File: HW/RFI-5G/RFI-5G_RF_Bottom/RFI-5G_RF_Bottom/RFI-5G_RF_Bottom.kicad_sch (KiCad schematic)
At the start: 20 parts, among them J1 Conn_01x10, J2 Conn_01x10, J3 Conn_01x10, J4 Conn_01x10, J5 SMP, J6 Conn_01x04_Female

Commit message: RF top and Bottom boards
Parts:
- removed J1, J2, J3: Conn_01x10, symbol Connector_Generic:Conn_01x10
- removed J6: Conn_01x04_Female, Connector_PinHeader_2.54mm:PinHeader_1x04_P2.54mm_Vertical, symbol Connector:Conn_01x04_Female
- removed U?: LEE2-6+, Package_SON:WSON-6-1EP_2x2mm_P0.65mm_EP1x1.6mm, symbol GGS_RF:LEE2-6+
- added C1, C5: 100nF, Capacitor_SMD:C_0402_1005Metric, symbol Device:C
- added C10, C6: 1uF, Capacitor_SMD:C_0402_1005Metric, symbol Device:C
- added C11, C12, C2, C4, C7: 10nF, Capacitor_SMD:C_0402_1005Metric, symbol Device:C
- added C18: 10uF, Capacitor_SMD:C_0402_1005Metric, symbol Device:C
- added FL1: LFCW-8400+, GGS_RF:JC0603C-1, symbol GGS_RF:LFCW-8000+
- added FL2: HFCN-5500+, GGS_RF:JC0603C, symbol GGS_RF:HFCN-5500+
- added FL3: SAW_869, GGS_RF:QCS5P, symbol GGS_RF:SAW_869
- added J1, J3: Conn_01x03, Connector_PinHeader_2.54mm:PinHeader_1x03_P2.54mm_Vertical, symbol Connector_Generic:Conn_01x03
- added J2: Conn_01x02, Connector_PinHeader_2.54mm:PinHeader_1x02_P2.54mm_Vertical, symbol Connector_Generic:Conn_01x02
- added J6: Conn_01x06_Female, Connector_PinHeader_1.00mm:PinHeader_1x06_P1.00mm_Vertical, symbol Connector:Conn_01x06_Female
- added L1: 0.9uH, Inductor_SMD:L_0603_1608Metric, symbol Device:L
- added L2: 590nH, Inductor_SMD:L_0603_1608Metric, symbol Device:L
- added L3: 120nH, Inductor_SMD:L_0603_1608Metric, symbol Device:L
- added R1: 3k, Resistor_SMD:R_0603_1608Metric, symbol Device:R
- added R2: 43R, Resistor_SMD:R_0603_1608Metric, symbol Device:R
- added R3: 88R7, Resistor_SMD:R_0603_1608Metric, symbol Device:R
- added U1: HMC8411, GGS_RF:6-LFCSP, symbol GGS_RF:HMC8411
- added U2: SIM-14+, GGS_RF:HV1195, symbol GGS_RF:SIM-14+
- added U4: LEE2-6+, Package_SON:WSON-6-1EP_2x2mm_P0.65mm_EP1x1.6mm, symbol GGS_RF:LEE2-6+
- added U7: HMC358, Package_SO:MSOP-8-1EP_3x3mm_P0.65mm_EP2.5x3mm_Mask1.73x2.36mm, symbol GGS_RF:HMC358
- C8: renamed from C?; value C -> 1uF
- C9: renamed from C?; value C -> 10nF
- J4: footprint (none) -> Connector_PinHeader_2.54mm:PinHeader_1x10_P2.54mm_Vertical
- J5: footprint easyeda:CES-110-XX-Y-S -> GGS_Connectors:SMP_StraightPlugPCB
- L4: renamed from L?; value L -> 120nH; footprint (none) -> Inductor_SMD:L_0603_1608Metric
- L5: renamed from L?; footprint (none) -> Inductor_SMD:L_0603_1608Metric
- R4: renamed from R?; value R -> 88R7; footprint (none) -> Resistor_SMD:R_0603_1608Metric
- R5: renamed from R?; footprint (none) -> Resistor_SMD:R_0603_1608Metric
- gave numbers to parts that had none: 7
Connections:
- net CHGOFF is gone; now on net Vcc_IF2Amp2: J4.7 (Pin_7)
- net CLPROG is gone; now on net 3V: J4.8 (Pin_8)
- net MPPT_X is gone; now on net RSSI_Out: J4.9 (Pin_9)
- net SOLAR_X is gone; now on net GND: J4.10 (Pin_10)
- net SWCLK is gone; now on net GND: J4.4 (Pin_4)
- net ADC_PL2: now also J3.2 (Pin_2); no longer J4.2 (Pin_2)
- net DAC_PL2: now also J3.3 (Pin_3); no longer J4.3 (Pin_3)
- net GND: now also J4.3 (Pin_3), U5.1 (NC), U5.3 (NC), U5.4 (NC), U5.6 (NC), U5.7 (NC), C1.1, C10.1, C11.1, C18.1, C2.1, C5.1, C6.1, C7.1, FL1.2 (GND), FL1.4 (GND), FL2.2 (GND), FL2.4 (GND), FL2.5 (GND), FL2.6 (GND), FL3.2 (GND), FL3.3 (GND), FL3.5 (GND), J1.3 (Pin_3), J2.1 (Pin_1), J3.1 (Pin_1), U1.3 (NC), U1.4 (NC), U1.6 (GND), U2.1 (GND), U4.1 (NC), U4.3 (NC), U4.4 (NC), U4.6 (NC), U4.7 (NC), U7.2 (NC), U7.4 (GND), U7.5 (GND), U7.6 (NC), U7.7 (NC), U7.9 (GND)
- net SCL: now also J1.2 (Pin_2)
- net SDA: now also J1.1 (Pin_1)
- net VCC: now also J2.2 (Pin_2)
- net LEE_2_Out: now reaches C13.1, L4.2, U5.5 (Out&DCin)
- net Vcc_IF2Amp2: now reaches C8.2, C9.2, R4.1
- net 3V: now reaches U3.1 (ENBL)
- net 3V: now also U3.6 (VCC), C10.2, C11.2
- net RSSI_In+: now reaches C14.2, U3.2 (IN+)
- net RSSI_IN-: now reaches C17.2, U3.3 (IN-)
- net RSSI_Out: now reaches U3.8 (OUT)
- net SAW_Out: now reaches U5.2 (In)
- net SAW_Out: now also FL3.4 (Out)
- net NRST renamed Vcc_IF2Amp1
- net Vcc_IF2Amp1: now also C6.2, C7.2, R3.1
- net PCLK renamed Vcc_VCO
- net Vcc_VCO: now also C18.2, J6.6 (Pin_6), U7.1 (Vcc)
- net RF_Bottom_In renamed IF1_In
- net IF1_In: now also FL2.1 (In)
- net SWIO renamed PoL
- new net: L3.1, R3.2
- new net: L2.2, R2.1
- new net: C5.2, R2.2
- new net: R1.2, U1.1 (RBIAS)
- new net IF1_Amp_Out: C4.1, L1.2, U1.5 (RFOut)
- new net IF1_HPF_Out: FL2.3 (Out), L2.1, U1.2 (RFIn)
- new net IF1_LPF_In: C4.2, FL1.1 (In)
- new net IF1_Out: FL1.3 (Out), U2.4 (RF)
- new net IF2_Amp1_Out: C12.1, L3.2, U4.5 (Out&DCin)
- new net LO2: U2.8 (LO), U7.8 (RFOut)
- new net Mixer_Out: U2.2 (IF), U4.2 (In)
- new net SAW_In: C12.2, FL3.1 (In)
- new net VTune1: J6.1 (Pin_1)
- new net VTune2: J4.2 (Pin_2), U7.3 (VTune)
- new net Vcc_IF1Amp: C1.2, C2.2, J6.3 (Pin_3), L1.1, R1.1
- new net Vcc_LNA1: J6.4 (Pin_4)
- new net Vcc_LNA2: J6.5 (Pin_5)
- new net Vcc_LO1Amp: J6.2 (Pin_2)
- no-connect marks 11 -> 0
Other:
- note added: "IF 1"
- note added: "IF 2"
- note added: "Local Oscillator 2"
- note added: "PoquetQube Connectors"
- note added: "RF Connector"
- note added: "Through-board Pins"
- moved on the sheet: C13, C14, C15, C16, C17, C8, C9, J5, L4, L5, R4, R5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

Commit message: PL boards
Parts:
- removed J6: Conn_01x06_Female, Connector_PinHeader_1.00mm:PinHeader_1x06_P1.00mm_Vertical, symbol Connector:Conn_01x06_Female
- added J6: Conn_01x10_Female, Connector_PinHeader_1.00mm:PinHeader_1x10_P1.00mm_Vertical, symbol Connector:Conn_01x10_Female
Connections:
- net 3V: now also J6.8 (Pin_8)
- net GND: now also J6.7 (Pin_7)
- net SCL: now also J6.10 (Pin_10)
- net SDA: now also J6.9 (Pin_9)
- net VTune1: now also J6.2 (Pin_2)
- net Vcc_IF1Amp: now also J6.1 (Pin_1)
- net Vcc_LNA1: now also J6.6 (Pin_6)
- net Vcc_LNA2: now also J6.5 (Pin_5)
- net Vcc_LO1Amp: now also J6.4 (Pin_4)
- net Vcc_VCO: now also J6.3 (Pin_3)
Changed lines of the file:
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@@
+    (stroke (width 0) (type default) (color 0 0 0 0))
+  )
+  (wire (pts (xy 104.14 148.59) (xy 111.76 148.59))
     (stroke (width 0) (type default) (color 0 0 0 0))
   )
@@
     (effects (font (size 1.27 1.27)) (justify left bottom))
   )
-  (global_label "Vcc_LO1Amp" (shape input) (at 113.03 139.7 180) (fields_autoplaced)
-    (effects (font (size 1.27 1.27)) (justify right))
-    (property "Intersheet References" "${INTERSHEET_REFS}" (id 0) (at 98.8845 139.6206 0)
+  (global_label "3V" (shape input) (at 111.76 151.13 180) (fields_autoplaced)
+    (effects (font (size 1.27 1.27)) (justify right))
+    (property "Intersheet References" "${INTERSHEET_REFS}" (id 0) (at 107.0488 151.0506 0)
       (effects (font (size 1.27 1.27)) (justify right) hide)
     )
@@
     )
   )
-  (global_label "Vcc_IF1Amp" (shape input) (at 113.03 142.24 180) (fields_autoplaced)
-    (effects (font (size 1.27 1.27)) (justify right))
-    (property "Intersheet References" "${INTERSHEET_REFS}" (id 0) (at 99.5498 142.1606 0)
-      (effects (font (size 1.27 1.27)) (justify right) hide)
-    )
-  )
-  (global_label "Vcc_VCO" (shape input) (at 113.03 149.86 180) (fields_autoplaced)
-    (effects (font (size 1.27 1.27)) (justify right))
-    (property "Intersheet References" "${INTERSHEET_REFS}" (id 0) (at 102.6945 149.7806 0)
-      (effects (font (size 1.27 1.27)) (justify right) hide)
-    )
-  )
   (global_label "IF1_In" (shape input) (at 76.2 39.37 180) (fields_autoplaced)
     (effects (font (size 1.27 1.27)) (justify right))
@@
     )
   )
-  (global_label "Vcc_LNA1" (shape input) (at 113.03 144.78 180) (fields_autoplaced)
-    (effects (font (size 1.27 1.27)) (justify right))
-    (property "Intersheet References" "${INTERSHEET_REFS}" (id 0) (at 101.7269 144.7006 0)
-      (effects (font (size 1.27 1.27)) (justify right) hide)
-    )
-  )
   (global_label "PoL" (shape input) (at 49.53 176.53 90) (fields_autoplaced)
     (effects (font (size 1.27 1.27)) (justify left))
@@
     )
   )
+  (global_label "Vcc_LNA2" (shape input) (at 111.76 143.51 180) (fields_autoplaced)
+    (effects (font (size 1.27 1.27)) (justify right))
+    (property "Intersheet References" "${INTERSHEET_REFS}" (id 0) (at 100.4569 143.4306 0)
+      (effects (font (size 1.27 1.27)) (justify right) hide)
+    )
+  )
   (global_label "Vcc_VCO" (shape input) (at 220.98 137.16 180) (fields_autoplaced)
     (effects (font (size 1.27 1.27)) (justify right))
@@
     )
   )
+  (global_label "Vcc_LNA1" (shape input) (at 111.76 146.05 180) (fields_autoplaced)
+    (effects (font (size 1.27 1.27)) (justify right))
+    (property "Intersheet References" "${INTERSHEET_REFS}" (id 0) (at 100.4569 145.9706 0)
+      (effects (font (size 1.27 1.27)) (justify right) hide)
+    )
+  )
   (global_label "IF1_In" (shape input) (at 165.1 139.7 180) (fields_autoplaced)
     (effects (font (size 1.27 1.27)) (justify right))
@@
     )
   )
-  (global_label "Vcc_LNA2" (shape input) (at 113.03 147.32 180) (fields_autoplaced)
-    (effects (font (size 1.27 1.27)) (justify right))
-    (property "Intersheet References" "${INTERSHEET_REFS}" (id 0) (at 101.7269 147.2406 0)
-      (effects (font (size 1.27 1.27)) (justify right) hide)
-    )
-  )
   (global_label "SDA" (shape bidirectional) (at 39.37 139.7 270) (fields_autoplaced)
     (effects (font (size 1.27 1.27)) (justify right))
@@
     )
   )
+  (global_label "VTune1" (shape input) (at 111.76 135.89 180) (fields_autoplaced)
+    (effects (font (size 1.27 1.27)) (justify right))
+    (property "Intersheet References" "${INTERSHEET_REFS}" (id 0) (at 102.6945 135.8106 0)
+      (effects (font (size 1.27 1.27)) (justify right) hide)
+    )
+  )
   (global_label "Vcc_IF2Amp2" (shape input) (at 156.21 77.47 180) (fields_autoplaced)
     (effects (font (size 1.27 1.27)) (justify right))
     (property "Intersheet References" "${INTERSHEET_REFS}" (id 0) (at 141.5202 77.3906 0)
+      (effects (font (size 1.27 1.27)) (justify right) hide)
+    )
+  )
+  (global_label "SCL" (shape bidirectional) (at 111.76 156.21 180) (fields_autoplaced)
+    (effects (font (size 1.27 1.27)) (justify right))
+    (property "Intersheet References" "${INTERSHEET_REFS}" (id 0) (at 105.8393 156.1306 0)
       (effects (font (size 1.27 1.27)) (justify right) hide)
     )
@@
     )
   )
+  (global_label "Vcc_LO1Amp" (shape input) (at 111.76 140.97 180) (fields_autoplaced)
+    (effects (font (size 1.27 1.27)) (justify right))
+    (property "Intersheet References" "${INTERSHEET_REFS}" (id 0) (at 97.6145 140.8906 0)
+      (effects (font (size 1.27 1.27)) (justify right) hide)
+    )
+  )
+  (global_label "Vcc_VCO" (shape input) (at 111.76 138.43 180) (fields_autoplaced)
+    (effects (font (size 1.27 1.27)) (justify right))
+    (property "Intersheet References" "${INTERSHEET_REFS}" (id 0) (at 101.4245 138.3506 0)
+      (effects (font (size 1.27 1.27)) (justify right) hide)
+    )
+  )
   (global_label "LO2" (shape input) (at 30.48 116.84 180) (fields_autoplaced)
     (effects (font (size 1.27 1.27)) (justify right))
@@
     )
   )
-  (global_label "VTune1" (shape input) (at 113.03 137.16 180) (fields_autoplaced)
-    (effects (font (size 1.27 1.27)) (justify right))
-    (property "Intersheet References" "${INTERSHEET_REFS}" (id 0) (at 103.9645 137.0806 0)
+  (global_label "SDA" (shape bidirectional) (at 111.76 153.67 180) (fields_autoplaced)
+    (effects (font (size 1.27 1.27)) (justify right))
+    (property "Intersheet References" "${INTERSHEET_REFS}" (id 0) (at 105.7788 153.5906 0)
       (effects (font (size 1.27 1.27)) (justify right) hide)
     )
@@
     (effects (font (size 1.27 1.27)) (justify right))
     (property "Intersheet References" "${INTERSHEET_REFS}" (id 0) (at 48.8102 77.3906 0)
+      (effects (font (size 1.27 1.27)) (justify right) hide)
+    )
+  )
+  (global_label "Vcc_IF1Amp" (shape input) (at 111.76 133.35 180) (fields_autoplaced)
+    (effects (font (size 1.27 1.27)) (justify right))
+    (property "Intersheet References" "${INTERSHEET_REFS}" (id 0) (at 98.2798 133.2706 0)
       (effects (font (size 1.27 1.27)) (justify right) hide)
     )
@@
     )
     (property "Datasheet" "" (id 3) (at 137.16 110.49 0)
+      (effects (font (size 1.27 1.27)) hide)
+    )
+    (pin "1")
+  )
+  (symbol (lib_id "power:GND") (at 104.14 148.59 270) (unit 1)
+    (in_bom yes) (on_board yes)
+    (property "Reference" "#PWR0107" (id 0) (at 97.79 148.59 0)
+      (effects (font (size 1.27 1.27)) hide)
+    )
+    (property "Value" "GND" (id 1) (at 99.06 147.32 0)
+      (effects (font (size 1.27 1.27)) (justify left))
+    )
+    (property "Footprint" "" (id 2) (at 104.14 148.59 0)
+      (effects (font (size 1.27 1.27)) hide)
+    )
+    (property "Datasheet" "" (id 3) (at 104.14 148.59 0)
       (effects (font (size 1.27 1.27)) hide)
     )
@@
     (pin "1")
   )
-  (symbol (lib_id "Connector:Conn_01x06_Female") (at 118.11 142.24 0) (unit 1)
-    (in_bom yes) (on_board yes) (fields_autoplaced)
-    (property "Reference" "J6" (id 0) (at 119.38 143.5099 0)
-      (effects (font (size 1.27 1.27)) (justify left))
-    )
-    (property "Value" "Conn_01x06_Female" (id 1) (at 119.38 144.7799 0)
-      (effects (font (size 1.27 1.27)) (justify left) hide)
-    )
-    (property "Footprint" "Connector_PinHeader_1.00mm:PinHeader_1x06_P1.00mm_Vertical" (id 2) (at 118.11 142.24 0)
-      (effects (font (size 1.27 1.27)) hide)
-    )
-    (property "Datasheet" "~" (id 3) (at 118.11 142.24 0)
-      (effects (font (size 1.27 1.27)) hide)
-    )
-    (pin "1")
-    (pin "2")
-    (pin "3")
-    (pin "4")
-    (pin "5")
-    (pin "6")
-  )
   (symbol (lib_id "power:GND") (at 222.25 85.09 0) (unit 1)
     (in_bom yes) (on_board yes) (fields_autoplaced)
@@
     (pin "1")
   )
+  (symbol (lib_id "Connector:Conn_01x10_Female") (at 116.84 143.51 0) (unit 1)
+    (in_bom yes) (on_board yes)
+    (property "Reference" "J6" (id 0) (at 113.03 129.54 0)
+      (effects (font (size 1.27 1.27)) (justify left))
+    )
+    (property "Value" "Conn_01x10_Female" (id 1) (at 118.11 146.0499 0)
+      (effects (font (size 1.27 1.27)) (justify left) hide)
+    )
+    (property "Footprint" "Connector_PinHeader_1.00mm:PinHeader_1x10_P1.00mm_Vertical" (id 2) (at 116.84 143.51 0)
+      (effects (font (size 1.27 1.27)) hide)
+    )
+    (property "Datasheet" "~" (id 3) (at 116.84 143.51 0)
+      (effects (font (size 1.27 1.27)) hide)
+    )
+    (pin "1")
+    (pin "10")
+    (pin "2")
+    (pin "3")
+    (pin "4")
+    (pin "5")
+    (pin "6")
+    (pin "7")
+    (pin "8")
+    (pin "9")
+  )
   (symbol (lib_id "power:GND") (at 59.69 144.78 0) (unit 1)
     (in_bom yes) (on_board yes) (fields_autoplaced)
@@
       (reference "#PWR0106") (unit 1) (value "GND") (footprint "")
     )
+    (path "/35519fd5-08ff-4fab-91c9-037e2a0c1c90"
+      (reference "#PWR0107") (unit 1) (value "GND") (footprint "")
+    )
     (path "/28b84f01-4b1c-4220-bcbc-a91fb9c17242"
       (reference "C1") (unit 1) (value "100nF") (footprint "Capacitor_SMD:C_0402_1005Metric")
@@
       (reference "J5") (unit 1) (value "SMP") (footprint "GGS_Connectors:SMP_StraightPlugPCB")
     )
-    (path "/bfa21043-576f-49ac-8f69-17c49a0821d4"
-      (reference "J6") (unit 1) (value "Conn_01x06_Female") (footprint "Connector_PinHeader_1.00mm:PinHeader_1x06_P1.00mm_Vertical")
+    (path "/f55b2315-ffcf-45cb-b8d5-dd0439b81933"
+      (reference "J6") (unit 1) (value "Conn_01x10_Female") (footprint "Connector_PinHeader_1.00mm:PinHeader_1x10_P1.00mm_Vertical")
     )
     (path "/6ba90c57-8775-4815-9ae3-5af56b73607e"

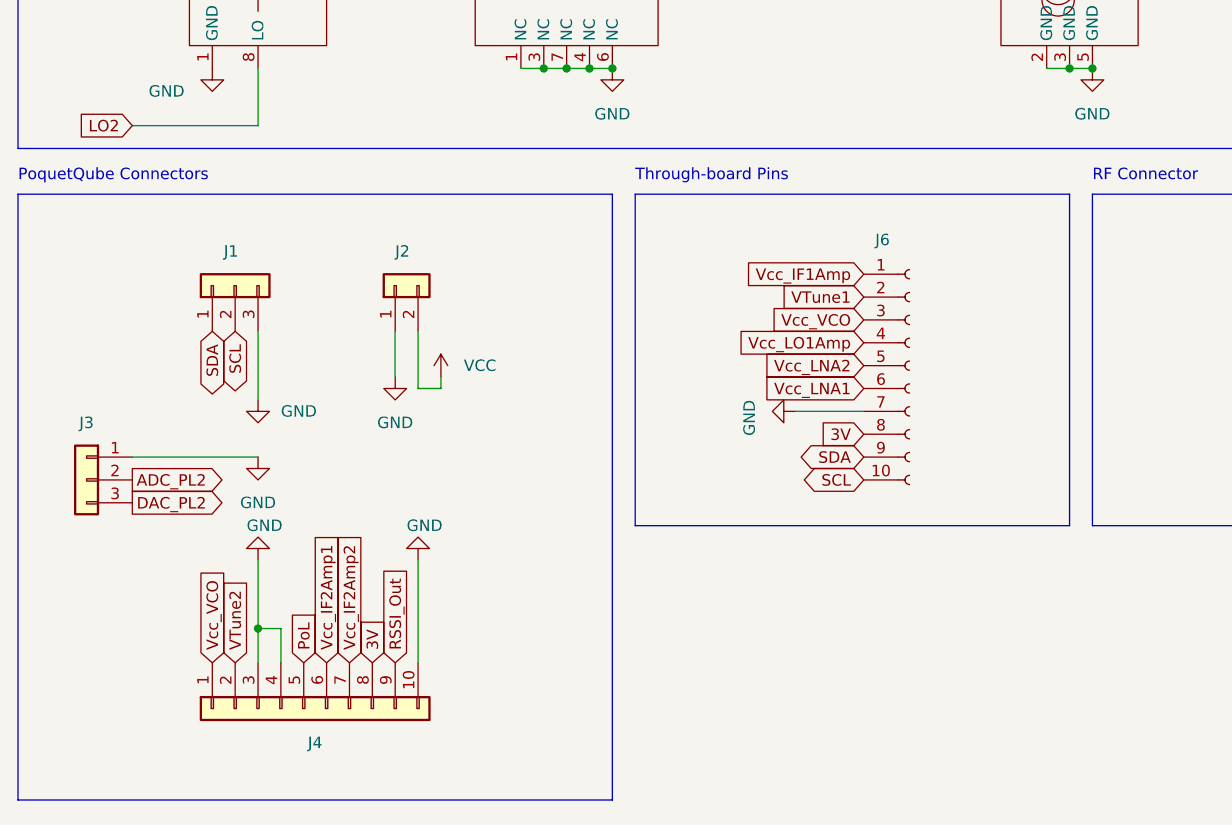
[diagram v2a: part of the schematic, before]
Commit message: All boards dseigned, thickness change pending
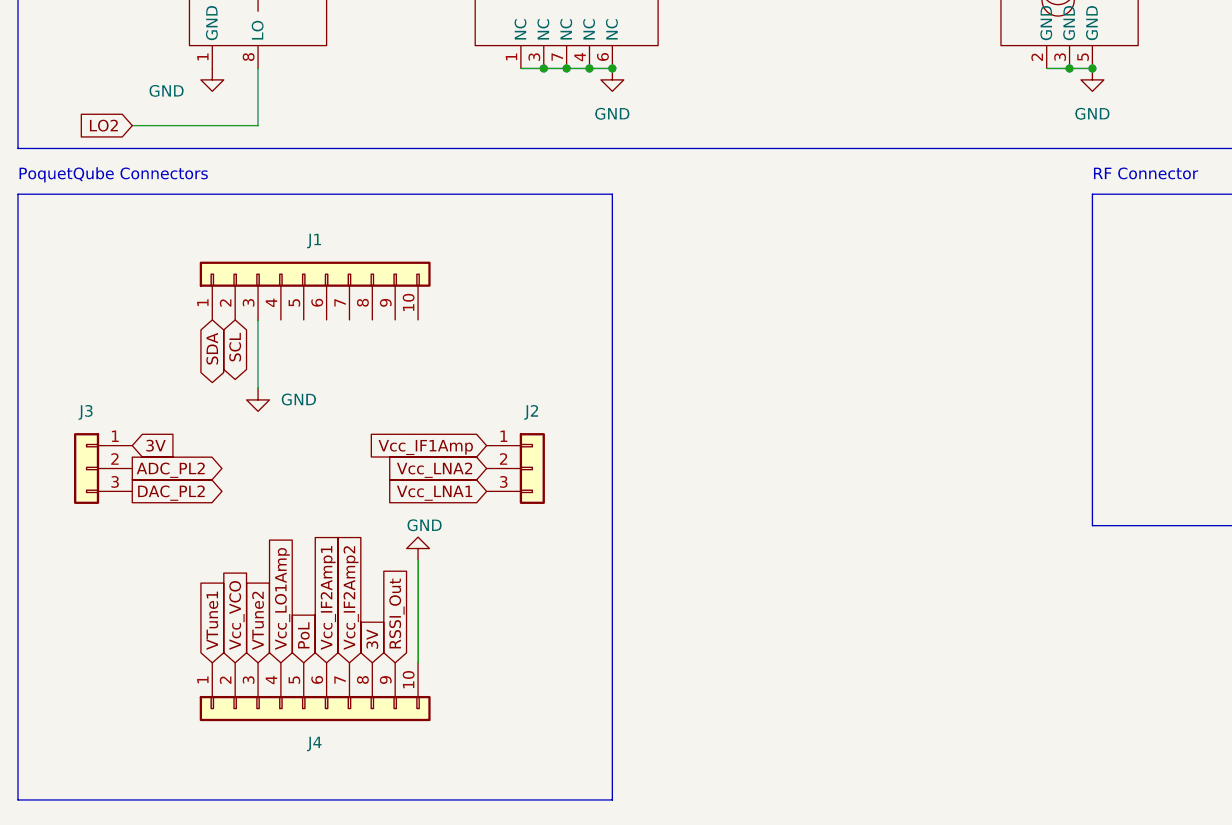
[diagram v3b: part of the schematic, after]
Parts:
- removed J1: Conn_01x03, Connector_PinHeader_2.54mm:PinHeader_1x03_P2.54mm_Vertical, symbol Connector_Generic:Conn_01x03
- removed J2: Conn_01x02, Connector_PinHeader_2.54mm:PinHeader_1x02_P2.54mm_Vertical, symbol Connector_Generic:Conn_01x02
- removed J6: Conn_01x10_Female, Connector_PinHeader_1.00mm:PinHeader_1x10_P1.00mm_Vertical, symbol Connector:Conn_01x10_Female
- added J1: Conn_01x10, Connector_PinHeader_2.54mm:PinHeader_1x10_P2.54mm_Vertical, symbol Connector_Generic:Conn_01x10
- added J2: Conn_01x03, Connector_PinHeader_2.54mm:PinHeader_1x03_P2.54mm_Vertical, symbol Connector_Generic:Conn_01x03
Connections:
- net 3V: now also J3.1 (Pin_1)
- net GND: now also J1.3 (Pin_3); no longer J3.1 (Pin_1), J4.3 (Pin_3), J4.4 (Pin_4)
- net SCL: now also J1.2 (Pin_2)
- net SDA: now also J1.1 (Pin_1)
- net VTune1: now also J4.1 (Pin_1)
- net VTune2: now also J4.3 (Pin_3); no longer J4.2 (Pin_2)
- net Vcc_IF1Amp: now also J2.1 (Pin_1)
- net Vcc_LNA1: now also J2.3 (Pin_3)
- net Vcc_LNA2: now also J2.2 (Pin_2)
- net Vcc_LO1Amp: now also J4.4 (Pin_4)
- net Vcc_VCO: now also J4.2 (Pin_2); no longer J4.1 (Pin_1)
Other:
- note removed: "Through-board Pins"
- moved on the sheet: J3
